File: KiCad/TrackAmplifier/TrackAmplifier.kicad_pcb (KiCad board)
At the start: 2 copper layers, 105 x 70 mm, 96 parts, among them J1 DB15_Male_MountingHoles, J2 Conn_01x06, Q1 2N7002, U1 ST485EBDR, U10 REF3025, U11 LM35-LP, U2 ST485EBDR, U3 LM78M05_TO252, U4 LMD18200, U5 ST485EBDR, U6 ST485EBDR, U7 INA326, U8 INA326, U9 PIC16F18854-SO

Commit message: Updated schematic and pcb.
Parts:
- removed R17: 0.2E, Resistor_THT:R_Axial_DIN0411_L9.9mm_D3.6mm_P12.70mm_Horizontal
- added R37: 10E, Resistor_SMD:R_1206_3216Metric, F.Cu at (118.6, 86.3)
- added REF**: ESD-Logo_13.2x12mm_SilkScreen, Symbol:ESD-Logo_13.2x12mm_SilkScreen, F.Cu at (111.0, 69.2)
- added REF**: KiCad-Logo2_6mm_SilkScreen, Symbol:KiCad-Logo2_6mm_SilkScreen, F.Cu at (56.4, 112.4)
- added REF**: OSHW-Logo2_14.6x12mm_SilkScreen, Symbol:OSHW-Logo2_14.6x12mm_SilkScreen, F.Cu at (56.4, 57.8)
- J2: footprint Connector_PinHeader_2.54mm:PinHeader_1x06_P2.54mm_Horizontal -> Connector_PinHeader_2.54mm:PinHeader_1x06_P2.54mm_Vertical; moved to F.Cu
- MK1: footprint MountingHole:MountingHole_3.7mm -> MountingHole:MountingHole_3.7mm_Pad_Via
- R16: value 0.2E -> 0.02; footprint Resistor_THT:R_Axial_DIN0411_L9.9mm_D3.6mm_P12.70mm_Horizontal -> Resistor_SMD:R_Shunt_2512_6332Metric_0.005-0.2
- U4: footprint Package_TO_SOT_THT:TO-220-11_Horizontal_TabDown_StaggeredType1_Py2.54mm -> Package_TO_SOT_THT:TO-220-11_20.02x17.50mm_P3.4x5.08mm_StaggerOdd_Lead8.45mm_Tab-Down
- moved R24 39.0 mm to (149.7, 81.3), turned to 270 degrees
- moved D1 5.08 mm to (130.6, 58.0)
- moved D2 5.08 mm to (133.8, 58.0)
- moved D3 5.08 mm to (137.0, 58.0)
- moved D4 5.08 mm to (140.2, 58.0)
- moved D8 5.08 mm to (143.3, 58.0)
- moved C16 4.45 mm to (111.0, 57.8)
- moved R16 4.07 mm to (104.6, 116.2)
- moved C17 4.07 mm to (149.7, 76.2), turned to 270 degrees
- moved R7 3.80 mm to (145.2, 70.5)
- moved R26 3.55 mm to (130.6, 62.9)
- moved R27 3.55 mm to (133.8, 62.9)
- moved R28 3.55 mm to (137.0, 62.9)
- moved R29 3.55 mm to (143.3, 62.9)
- moved R35 3.55 mm to (140.2, 62.9)
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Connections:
- C17 pad 2: OCC1 -> PWM1
- C21 pad 2: REF -> Net-(C21-Pad2)
- C25 pad 2: REF -> Net-(C25-Pad2)
- FL1 pad 1: OCC2 -> Net-(FL1-Pad1)
- FL2 pad 1: Net-(FL2-Pad1) -> GNDD
- J1 pad 15: Net-(FL2-Pad1) -> GNDD
- J1 pad 9: Net-(FL2-Pad1) -> GNDD
- R15 pad 1: REF -> VREF
- R15 pad 2: GND -> Net-(C21-Pad2)
- R16 pad 1: OCC1 -> PWM1
- R16 pad 2: OCC2 -> OCC1
- R21 pad 1: REF -> VREF
- R21 pad 2: GND -> Net-(C25-Pad2)
- U10 pad 2: REF -> VREF
- U11 pad 2: TEMP -> Net-(R37-Pad1)
- U4 pad 2: OCC1 -> PWM1
- U7 pad 3: OCC1 -> PWM1
- U7 pad 5: REF -> Net-(C21-Pad2)
- U8 pad 5: REF -> Net-(C25-Pad2)
- U9 pad 2: REF -> VREF
- U9 pad 3: REF -> VREF
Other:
- outline, holes or cut-outs redrawn
- board text added: "ERR"
- board text added: "RUN"
- board text added: "RX"
- board text added: "TX"
- board text added: "WAR"

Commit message: updated schematic
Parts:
- added C36: 220n, Capacitor_SMD:C_1206_3216Metric, F.Cu at (138.7, 110.9)
- added D10: 1n4148, Diode_SMD:D_1206_3216Metric, F.Cu at (133.1, 116.6)
- added D9: 1n4148, Diode_SMD:D_1206_3216Metric, F.Cu at (133.1, 110.9)
- added F1: Polyfuse, Fuse:Fuse_Bourns_MF-SM_7.98x5.44mm, F.Cu at (121.1, 54.5)
- added R17: 10k, Resistor_SMD:R_1206_3216Metric, F.Cu at (143.8, 110.9)
- added R38: 10E, Resistor_SMD:R_1206_3216Metric, F.Cu at (138.7, 116.6)
- C6: value 22u -> 470u; footprint Capacitor_THT:CP_Axial_L21.0mm_D8.0mm_P28.00mm_Horizontal -> Capacitor_THT:CP_Radial_D10.0mm_P5.00mm
- R16: value 0.02 -> 0.025
- moved C6 8.13 mm to (121.6, 62.1)
- moved REF** 7.55 mm to (116.0, 74.8)
- moved U10 1.13 mm to (88.9, 81.4)
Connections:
- C6 pad 1: Vbus_flt -> Net-(C6-Pad1)
- C8 pad 2: Vbus_flt -> Net-(C6-Pad1)
- C9 pad 2: Vbus_flt -> Net-(C6-Pad1)
- FL2 pad 4: Vbus_flt+ -> Vbus_flt
- R3 pad 1: Vbus_flt+ -> Vbus_flt
- U4 pad 6: Vbus_flt -> Net-(C6-Pad1)
- U9 pad 2: VREF -> ID
- U9 pad 3: VREF -> Net-(R38-Pad2)
- U9 pad 6: ID -> Vlm

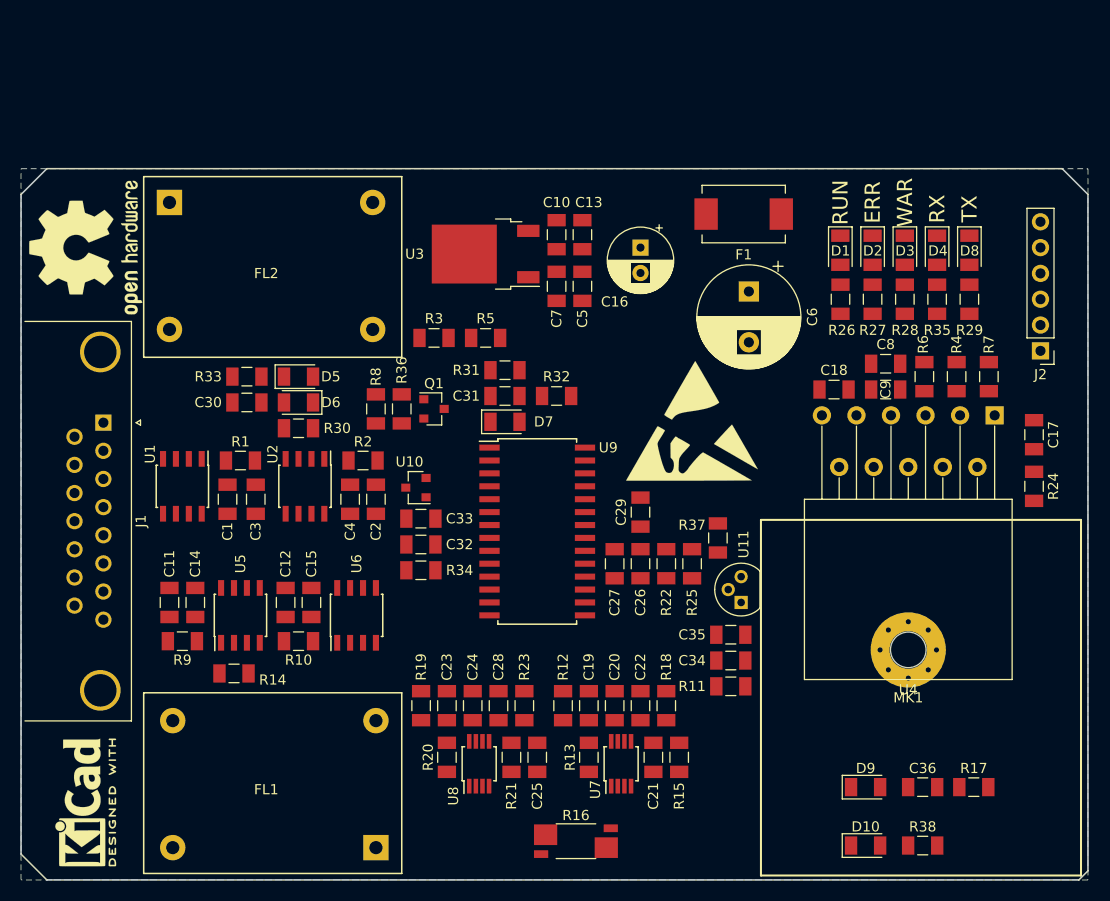
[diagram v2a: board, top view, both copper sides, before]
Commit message: update schematic
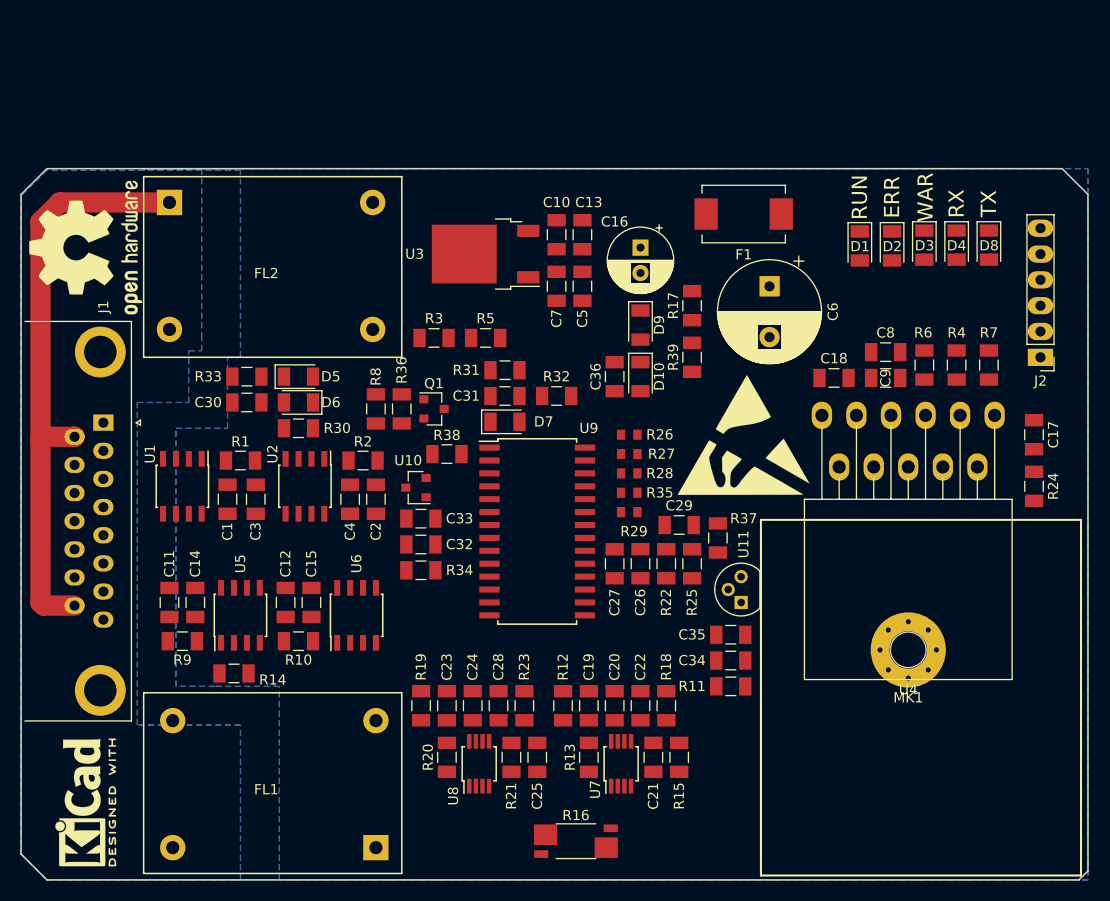
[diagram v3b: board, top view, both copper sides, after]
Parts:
- added R39: 50k, Resistor_SMD:R_1206_3216Metric, F.Cu at (116.0, 68.6)
- F1: value Polyfuse -> 3.0A
- R26, R27, R28, R29, R35: footprint Resistor_SMD:R_1206_3216Metric -> Resistor_SMD:R_0603_1608Metric
- moved R38 60.6 mm to (91.9, 78.1)
- moved R17 54.9 mm to (116.0, 63.5), turned to 90 degrees
- moved D10 51.2 mm to (111.0, 70.5), turned to 270 degrees
- moved D9 50.6 mm to (111.0, 65.4), turned to 270 degrees
- moved C36 50.5 mm to (108.4, 70.5), turned to 90 degrees
- moved R29 39.5 mm to (109.9, 83.8), turned to 180 degrees
- moved R35 35.8 mm to (109.9, 81.9), turned to 180 degrees
- moved R28 32.1 mm to (109.9, 80.0), turned to 0 degrees
- moved R27 28.4 mm to (109.9, 78.1), turned to 0 degrees
- moved R26 24.7 mm to (109.9, 76.2), turned to 180 degrees
- moved REF** 5.27 mm to (121.1, 76.2)
- moved C29 4.02 mm to (114.8, 85.1), turned to 180 degrees
- moved C6 2.09 mm to (123.7, 61.6)
- moved D3 1.99 mm to (138.9, 57.5)
- moved D4 1.99 mm to (142.1, 57.5)
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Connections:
- FL2 pad 1: GNDD -> Net-(FL2-Pad1)
- FL2 pad 2: GND -> Vbus_flt
- FL2 pad 3: Net-(FL2-Pad3) -> GNDD
- FL2 pad 4: Vbus_flt -> GND
- J1 pad 1: Net-(FL2-Pad3) -> GNDD
- J1 pad 15: GNDD -> Net-(FL2-Pad1)
- J1 pad 8: Net-(FL2-Pad3) -> GNDD
- J1 pad 9: GNDD -> Net-(FL2-Pad1)
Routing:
- net Net-(FL2-Pad1): track 0.00 -> 58.0 mm
- added copper zone on B.Cu, net GNDD

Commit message: updated PCB
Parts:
- C17, C18, C8, C9: moved to B.Cu
- R26, R27, R28, R29, R35: footprint Resistor_SMD:R_0603_1608Metric -> Resistor_SMD:R_1206_3216Metric
- moved R29 41.2 mm to (145.2, 62.7), turned to 90 degrees
- moved R35 37.5 mm to (142.1, 62.7), turned to 270 degrees
- moved REF** 36.2 mm to (111.6, 41.3)
- moved R28 33.8 mm to (138.9, 62.7), turned to 90 degrees
- moved R27 30.0 mm to (135.7, 62.9), turned to 90 degrees
- moved R26 26.3 mm to (132.6, 62.9), turned to 90 degrees
- moved R3 23.1 mm to (109.1, 52.7), turned to 180 degrees
- moved R14 20.9 mm to (90.6, 92.7)
- moved C8 20.2 mm to (140.2, 87.6), turned to 180 degrees
- moved C13 18.2 mm to (88.7, 64.1), turned to 270 degrees
- moved C5 17.5 mm to (88.7, 55.9), turned to 90 degrees
- moved R5 15.9 mm to (103.3, 52.7), turned to 180 degrees
- moved C9 15.3 mm to (140.2, 85.1), turned to 180 degrees
- moved C18 14.5 mm to (130.0, 85.1)
- moved C10 13.7 mm to (91.3, 64.1), turned to 270 degrees
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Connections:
- MK1 pad 1: (no net) -> GND
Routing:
- net GND: track 0.00 -> 76.4 mm, vias 0 -> 9
- net +5V: track 0.00 -> 61.2 mm, vias 0 -> 1
- net Net-(C6-Pad1): track 0.00 -> 58.6 mm
- net Vbus_flt: track 0.00 -> 43.5 mm, vias 0 -> 1
- net +15V: track 0.00 -> 23.1 mm
- net CSEN_FLT: track 0.00 -> 15.7 mm
- net Net-(C26-Pad2): track 0.00 -> 7.74 mm
- net Net-(C17-Pad1): track 0.00 -> 7.37 mm
- net Net-(C18-Pad2): track 0.00 -> 7.11 mm
- net PWM2: track 0.00 -> 4.86 mm
- net PWM1: track 0.00 -> 4.60 mm
- net Net-(R3-Pad2): track 0.00 -> 2.86 mm
- net Net-(FL2-Pad1): track 58.0 -> 56.1 mm
- added copper zone on F.Cu, net GND

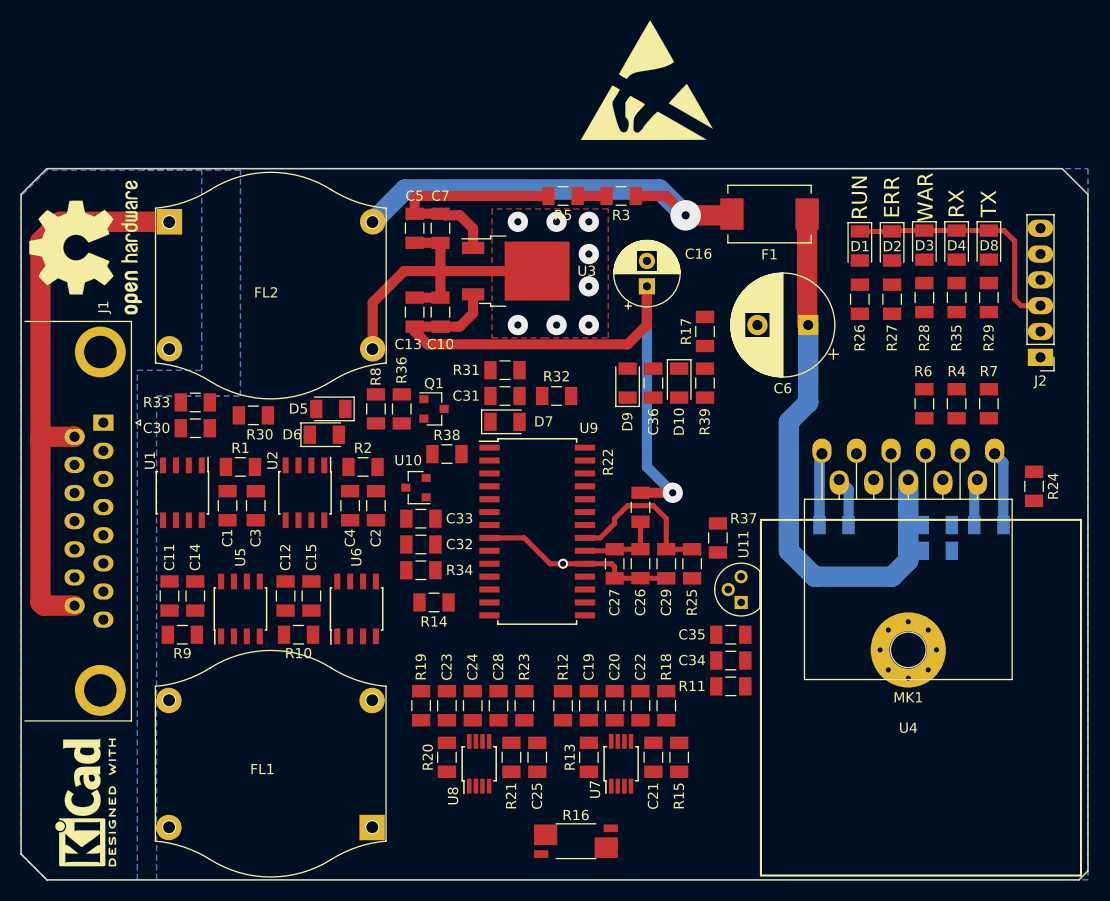
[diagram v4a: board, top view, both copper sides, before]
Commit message: TrackAmplifier.kicad_pcb finished To do: - Check and fit test
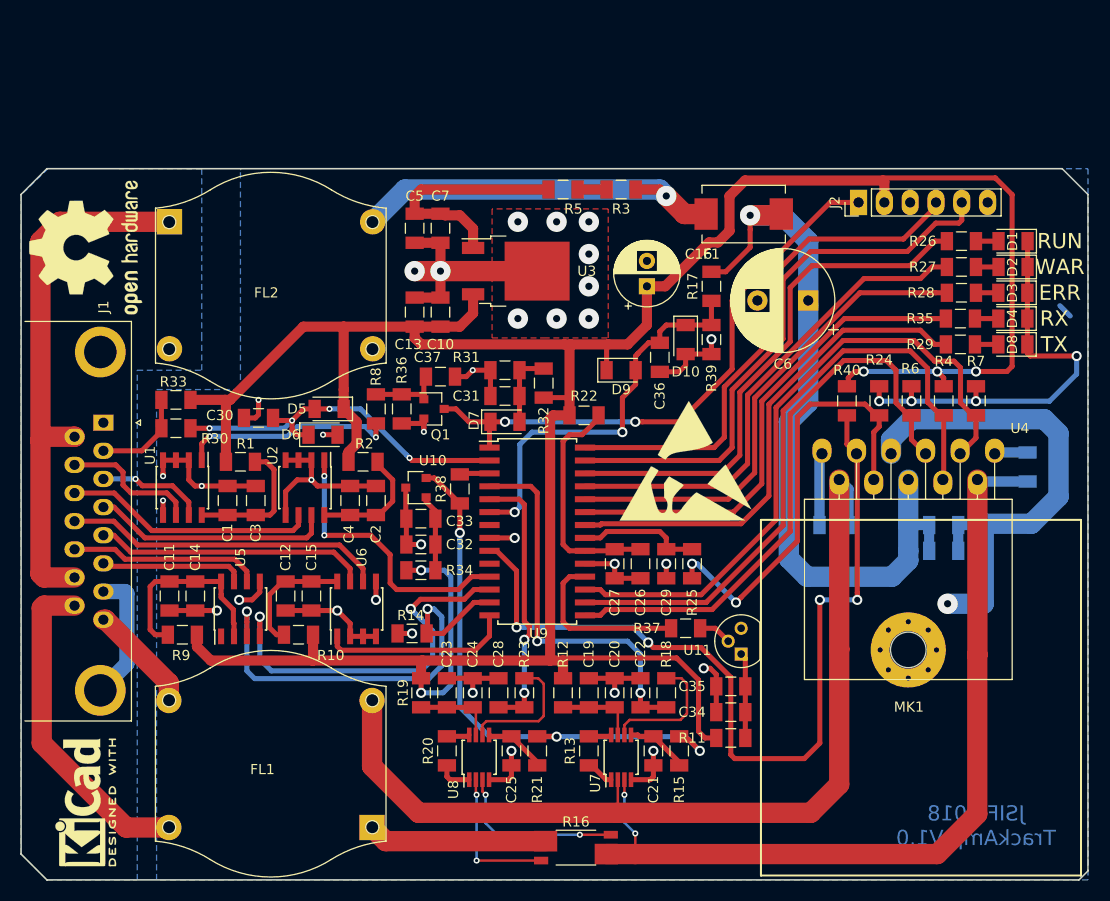
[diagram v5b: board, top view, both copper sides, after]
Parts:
- added C37: 100n, Capacitor_SMD:C_1206_3216Metric, F.Cu at (91.3, 70.5)
- added R40: 4k7, Resistor_SMD:R_1206_3216Metric, F.Cu at (131.3, 72.8)
- C30: value 22u -> 220n
- R30: value 1K -> 10k
- moved REF** 37.7 mm to (115.4, 78.7)
- moved J2 23.5 mm to (132.4, 53.3), turned to 90 degrees
- moved R24 17.4 mm to (134.5, 72.8)
- moved D1 15.1 mm to (147.6, 57.1), turned to 180 degrees
- moved D2 12.1 mm to (147.6, 59.7), turned to 180 degrees
- moved R26 11.5 mm to (142.6, 57.1), turned to 0 degrees
- moved R22 10.6 mm to (105.4, 74.3), turned to 0 degrees
- moved D8 10.1 mm to (147.6, 67.3), turned to 180 degrees
- moved D3 9.89 mm to (147.6, 62.2), turned to 180 degrees
- moved R37 9.44 mm to (115.4, 95.2), turned to 180 degrees
- moved D4 9.11 mm to (147.6, 64.8), turned to 180 degrees
- moved R30 7.73 mm to (65.2, 75.5)
- moved R27 7.53 mm to (142.6, 59.7), turned to 0 degrees
- moved C17 6.87 mm to (149.1, 79.4), turned to 270 degrees
- moved C30 6.31 mm to (73.4, 74.5), turned to 0 degrees
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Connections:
- C30 pad 2: ID_R -> ID
- J1 pad 13: TX_B -> TX_A
- J1 pad 14: PWMO1 -> Net-(FL2-Pad1)
- J1 pad 15: Net-(FL2-Pad1) -> PWMO1
- J1 pad 6: TX_A -> TX_B
- J1 pad 7: PWMO2 -> GNDD
- J1 pad 8: GNDD -> PWMO2
- U2 pad 2: Net-(U2-Pad2) -> GND
- U2 pad 3: Net-(U2-Pad2) -> GND
- U2 pad 4: Net-(U2-Pad2) -> GND
- U2 pad 5: Net-(U2-Pad2) -> GND
- U4 pad 9: Net-(U4-Pad9) -> THFLG
- U9 pad 15: DIR -> PWM
- U9 pad 17: PWM -> DIR
- U9 pad 9: Net-(U9-Pad9) -> THFLG
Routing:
- net +5V: track 61.2 -> 287.6 mm, vias 1 -> 5
- net GND: track 76.4 -> 237.9 mm, vias 9 -> 38
- net PWM2: track 4.86 -> 93.7 mm
- net THFLG: track 0.00 -> 85.9 mm, vias 0 -> 4
- net PWM1: track 4.60 -> 84.3 mm, vias 0 -> 2
- net DIR: track 0.00 -> 65.0 mm
- net BRK: track 0.00 -> 63.1 mm
- net PWM: track 0.00 -> 57.8 mm
- net RST: track 0.00 -> 56.8 mm, vias 0 -> 2
- net ICSPCLK: track 0.00 -> 55.4 mm
- net VREF: track 0.00 -> 54.3 mm, vias 0 -> 3
- net Net-(R26-Pad1): track 0.00 -> 51.9 mm
- net ICSPDAT: track 0.00 -> 51.3 mm
- net Net-(R29-Pad1): track 0.00 -> 49.3 mm
- net Net-(R27-Pad1): track 0.00 -> 48.5 mm
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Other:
- rule via_min_drill: 0.6 -> 0.3
- rule via_min_size: 1 -> 0.6
- board text added: "JSIF 2018 TrackAmp V1.0"
